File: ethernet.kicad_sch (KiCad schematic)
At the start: 12 parts, among them U3 SRV05-4, U4 SRV05-4

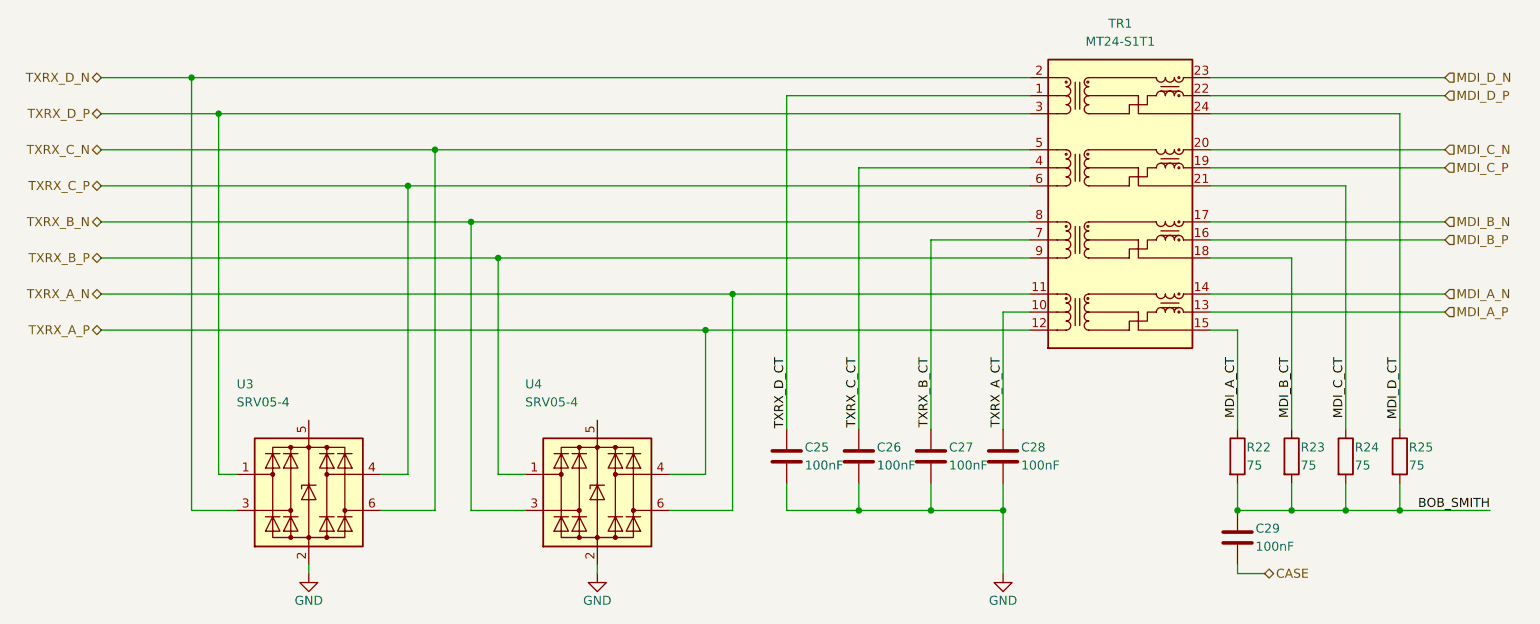
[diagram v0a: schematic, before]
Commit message: * ground plane change to keep out beneath the magnetic module * changed RJ45 modular jack from tab up to tab down to improve the routing * added an 3d modell in the library folder for the rj45 connector * added a fitting footprint for SS74800-038F * changed width of the MDI and MII tracks to the JLC3313 stackup * changed impedance of the pcie lane from 100 Ohm differential to 85 Ohm and from 50 single ended to 45 ohm * impedace calculation pictures still missing
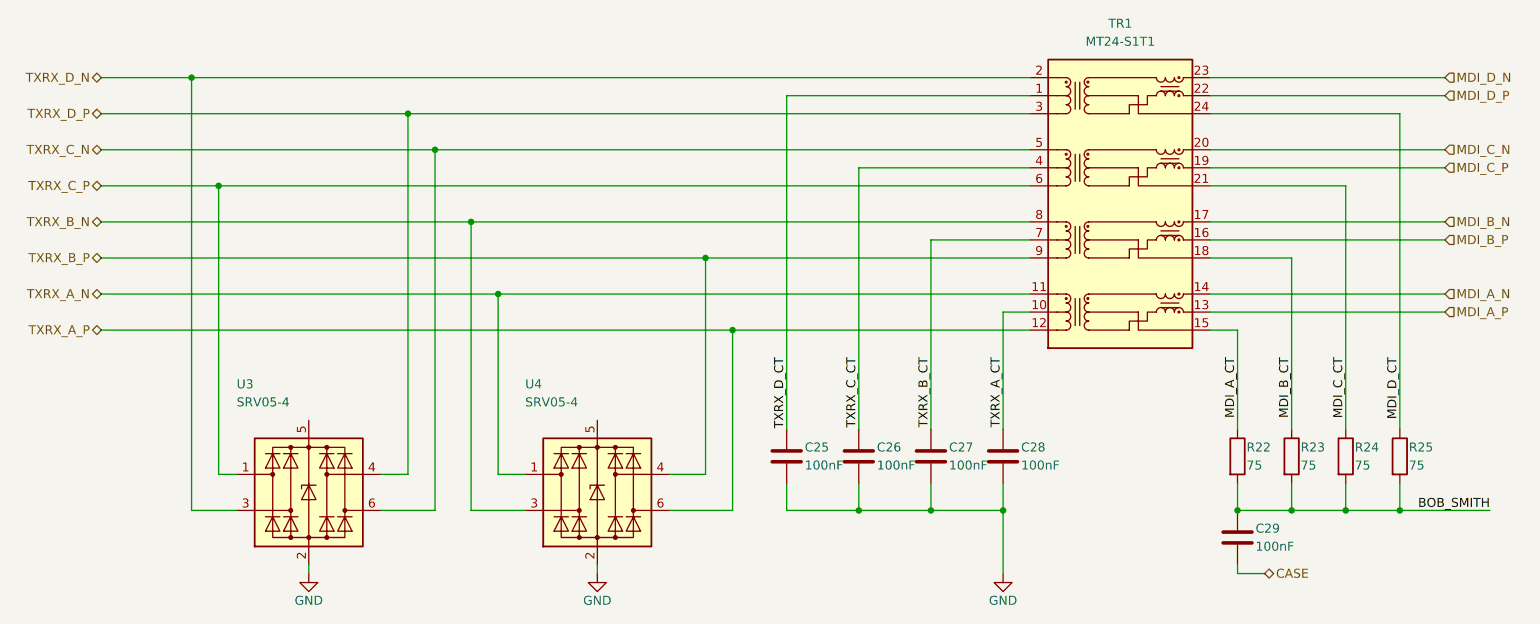
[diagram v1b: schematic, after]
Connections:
- net TXRX_A_N: now also U4.1 (I/O1); no longer U4.6 (I/O4)
- net TXRX_A_P: now also U4.6 (I/O4); no longer U4.4 (I/O3)
- net TXRX_B_P: now also U4.4 (I/O3); no longer U4.1 (I/O1)
- net TXRX_C_P: now also U3.1 (I/O1); no longer U3.4 (I/O3)
- net TXRX_D_P: now also U3.4 (I/O3); no longer U3.1 (I/O1)
